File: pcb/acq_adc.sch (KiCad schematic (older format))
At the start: 42 parts, among them J1 SMA, P2 A1, P7 EPV, Q1 2N7000, U1 LM7705, U2 MAX4477, U3 NCP700B, U4 MAX11102, U5 MAX6126BASA25+

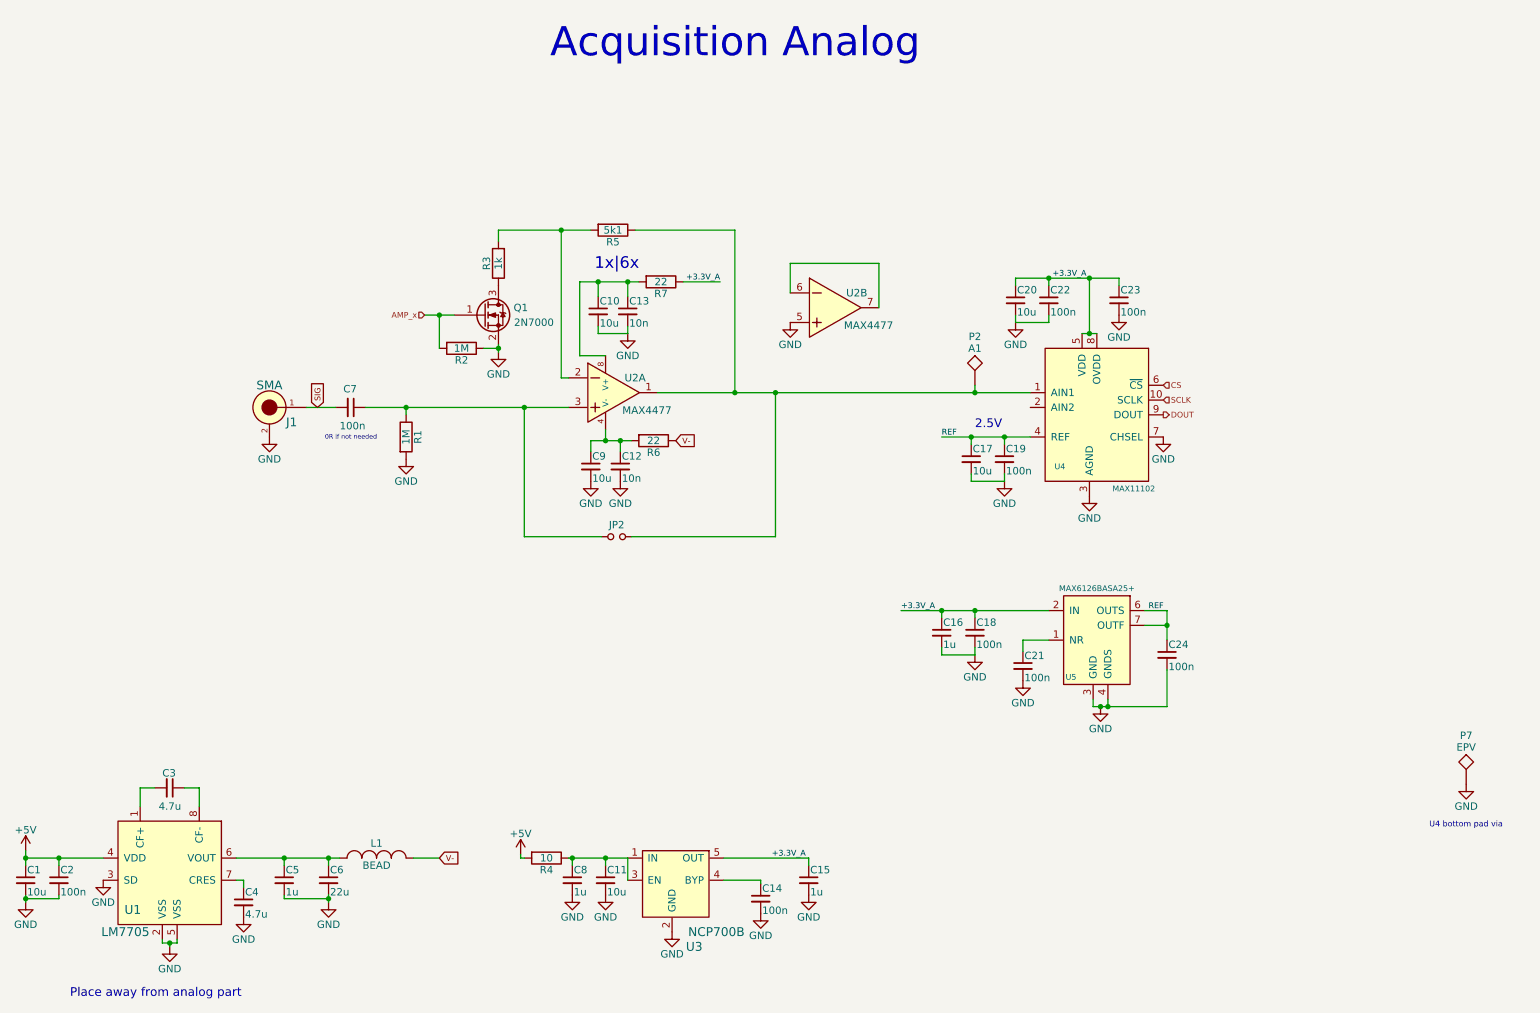
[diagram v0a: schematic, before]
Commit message: pcb: Update to v1.1
Changes:
 Add input protection diodes to acquisition board
 Add second screw hole to the preamplifier
 Add PCB revision number to the board
 LPF->HPF at the output of the preamplifier board
 Fix connector orientation on the preamplifier board
 Fix enclosure front/back PCBs
 Add constant amplification resistor to the acquisition board
 Switch the reference to 2.0V because MAX4477 has low maximal input common mode
 voltage
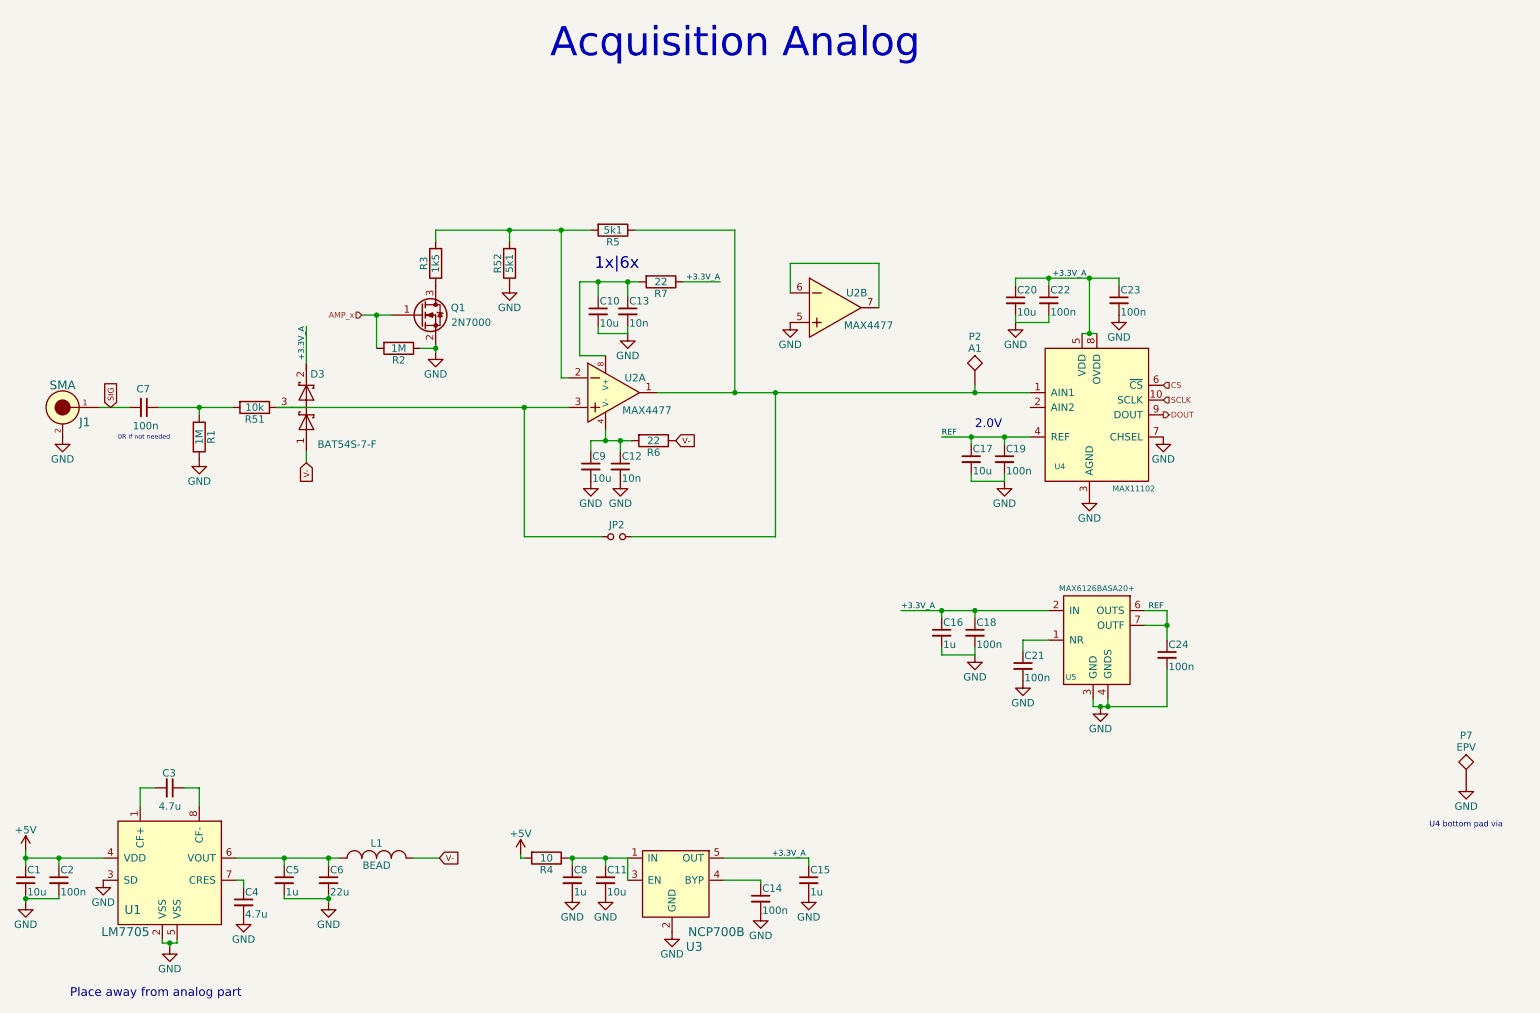
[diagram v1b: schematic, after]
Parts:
- added D3: BAT54S-7-F, TO_SOT_Packages_SMD:SOT-23, symbol D_Schottky_x2_Serial_AKC
- added R51: 10k, Resistors_SMD:R_0402, symbol R
- added R52: 5k1, Resistors_SMD:R_0402, symbol R
- R3: value 1k -> 1k5
- U5: value MAX6126BASA25+ -> MAX6126BASA20+
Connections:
- net +3.3V_A: now also D3.2 (K)
- net GND: now also R52.1
- net V-: now also D3.1 (A)
- net at R3.2, R5.2, U2.2: now also R52.2
- net at JP2.1, U2.3: now also D3.3 (common), R51.1; no longer C7.1, R1.1
- new net: C7.1, R1.1, R51.2
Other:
- note added: "2.0V"
- note removed: "2.5V"
- moved on the sheet: C7, J1, Q1, R1, R2, R3

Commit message: pcb: Update to the current iteration
Looks like I forgot to commit the changes made for manufacturing...
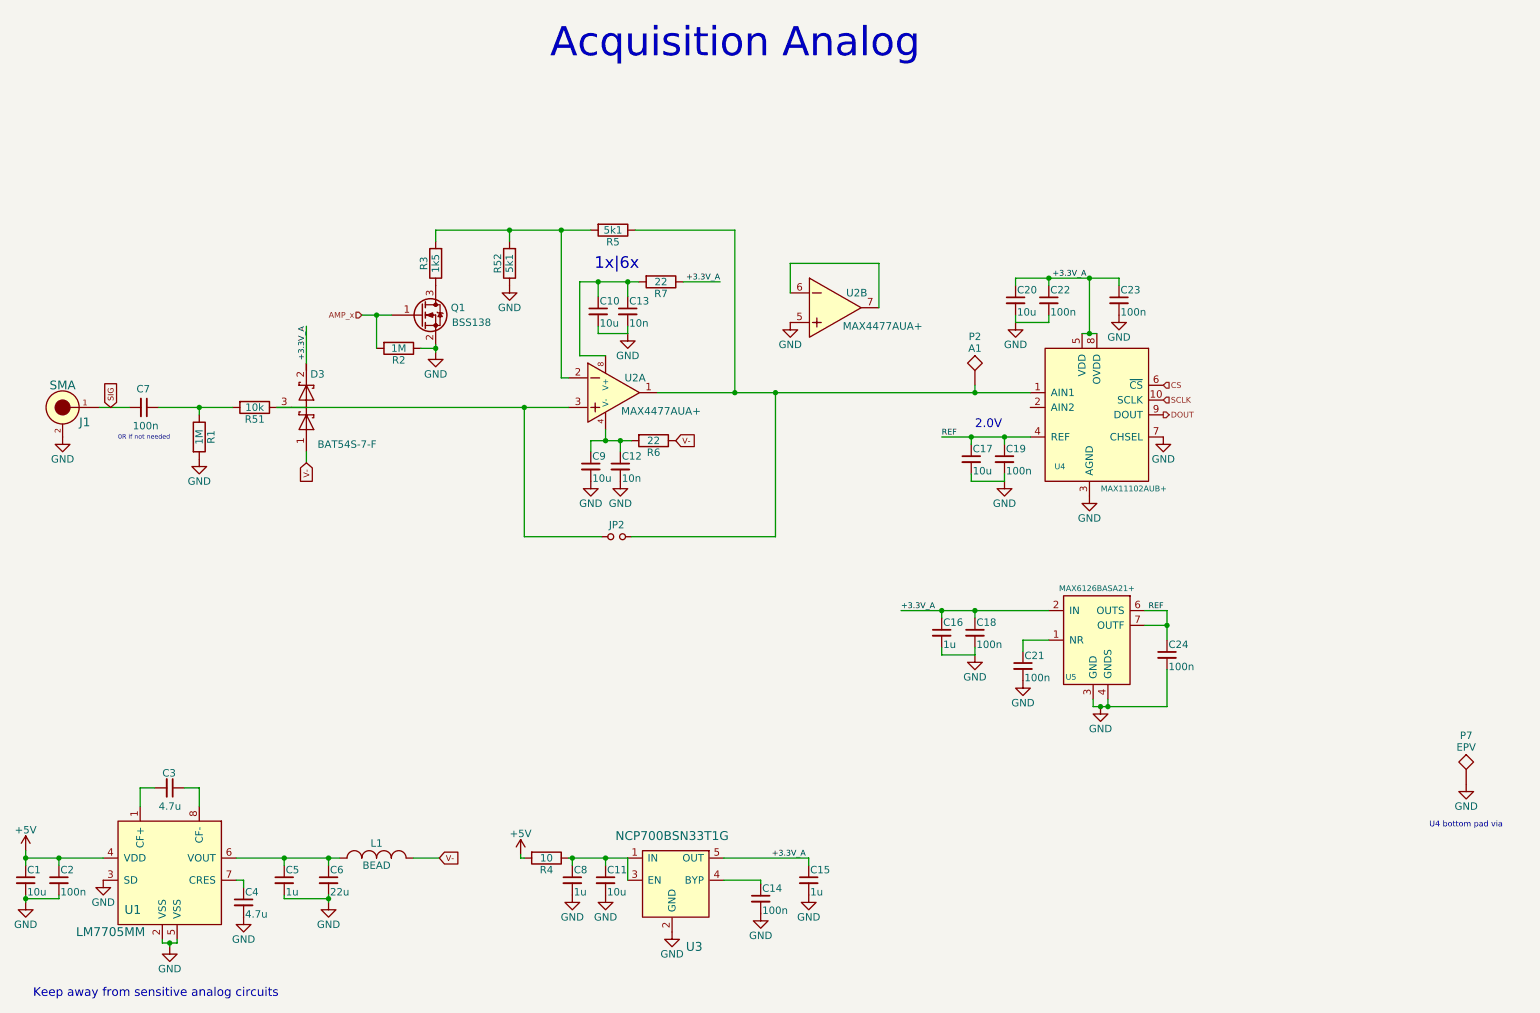
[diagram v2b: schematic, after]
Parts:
- JP2: value Jumper_NO_Small -> DNP
- Q1: value 2N7000 -> BSS138
- U1: value LM7705 -> LM7705MM
- U2: value MAX4477 -> MAX4477AUA+
- U3: value NCP700B -> NCP700BSN33T1G
- U4: value MAX11102 -> MAX11102AUB+
- U5: value MAX6126BASA20+ -> MAX6126BASA21+
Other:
- note added: "Keep away from sensitive analog circuits"
- note removed: "Place away from analog part"
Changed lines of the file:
@@
 EESchema Schematic File Version 2
+LIBS:pcb-rescue
 LIBS:power
 LIBS:device
@@
 P 4875 3300
 F 0 "U2" H 5075 3400 51  0000 C CNN
-F 1 "MAX4477" H 5155 3180 51  0000 C CNN
+F 1 "MAX4477AUA+" H 5250 3175 51  0000 C CNN
 F 2 "Housings_SSOP:MSOP-8_3x3mm_Pitch0.65mm" H 4765 2900 157 0001 C CNN
 F 3 "" H 4765 2900 157 0000 C CNN
@@
 P 4950 4275
 F 0 "JP2" H 4950 4355 50  0000 C CNN
-F 1 "Jumper_NO_Small" H 4960 4215 50  0001 C CNN
+F 1 "DNP" H 4960 4215 50  0001 C CNN
 F 2 "Resistors_SMD:R_0402" H 4950 4275 50  0001 C CNN
 F 3 "" H 4950 4275 50  0000 C CNN
@@
 P 6375 2725
 F 0 "U2" H 6575 2825 51  0000 C CNN
-F 1 "MAX4477" H 6655 2605 51  0000 C CNN
+F 1 "MAX4477AUA+" H 6750 2600 51  0000 C CNN
 F 2 "Housings_SSOP:MSOP-8_3x3mm_Pitch0.65mm" H 6265 2325 157 0001 C CNN
 F 3 "" H 6265 2325 157 0000 C CNN
@@
 P 5375 6600
 F 0 "U3" H 5475 6150 60  0000 C CNN
-F 1 "NCP700B" H 5625 6250 60  0000 C CNN
+F 1 "NCP700BSN33T1G" H 5325 6900 60  0000 C CNN
 F 2 "TO_SOT_Packages_SMD:SOT-23-5" H 6325 5850 60  0001 C CNN
 F 3 "" H 6325 5850 60  0000 C CNN
@@
 P 3625 2775
 F 0 "Q1" H 3925 2825 50  0000 R CNN
-F 1 "2N7000" H 4100 2725 50  0000 R CNN
+F 1 "BSS138" H 4100 2725 50  0000 R CNN
 F 2 "TO_SOT_Packages_SMD:SOT-23" H 3825 2875 50  0001 C CNN
 F 3 "" H 3625 2775 50  0000 C CNN
@@
 P 8225 4975
 F 0 "U5" H 8025 4725 39  0000 C CNN
-F 1 "MAX6126BASA20+" H 8200 5325 39  0000 C CNN
+F 1 "MAX6126BASA21+" H 8200 5325 39  0000 C CNN
 F 2 "Housings_SOIC:SOIC-8_3.9x4.9mm_Pitch1.27mm" H 7825 4625 20  0001 C CNN
 F 3 "" H 7825 4625 20  0000 C CNN
@@
 P 1875 6600
 F 0 "U1" H 1675 6400 60  0000 C CNN
-F 1 "LM7705" H 1625 6250 60  0000 C CNN
+F 1 "LM7705MM" H 1525 6250 60  0000 C CNN
 F 2 "Housings_SSOP:MSOP-8_3x3mm_Pitch0.65mm" H 1975 6450 60  0001 C CNN
 F 3 "" H 1975 6450 60  0000 C CNN
@@
 	1    0    0    -1
 $EndComp
-Text Notes 1250 7400 0    59   ~ 0
-Place away from analog part
+Text Notes 1000 7400 0    59   ~ 0
+Keep away from sensitive analog circuits
 Text GLabel 3750 6450 2    39   Input ~ 0
 V-
@@
 P 8200 3450
 F 0 "U4" H 7950 3100 39  0000 C CNN
-F 1 "MAX11102" H 8450 2950 39  0000 C CNN
+F 1 "MAX11102AUB+" H 8450 2950 39  0000 C CNN
 F 2 "footprints:uMAX-10-EP" H 8350 3450 20  0001 C CNN
 F 3 "" H 8350 3450 20  0000 C CNN
